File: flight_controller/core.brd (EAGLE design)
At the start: 94 x 90 mm, 102 parts, among them J1 M02, J13 MOLEX-3POS, J14 MOLEX-3POS, J15 MOLEX-4POS, J16 MOLEX-3POS, J17 M03, J18 M04, J19 MOLEX-3POS, J2 MOLEX-2POS, J20 MOLEX-4POS, J3 MOLEX-2POS, J4 MOLEX-2POS, J5 MOLEX-2POS, J6 MOLEX-2POS, J7 MOLEX-2POS, J8 MOLEX-2POS, J9 MOLEX-2POS, Q1 EM6K1, Q10 EM6K1, Q11 EM6K1, Q2 EM6K1, Q7 EM6K1, Q8 EM6K1, U1 MPU-6000QFN-24, U2 MEAS-MS5611, U3 USD-SOCKETNEW, U4 STM32F405, U5 MIC5219 3.3V, Y1 16MHz

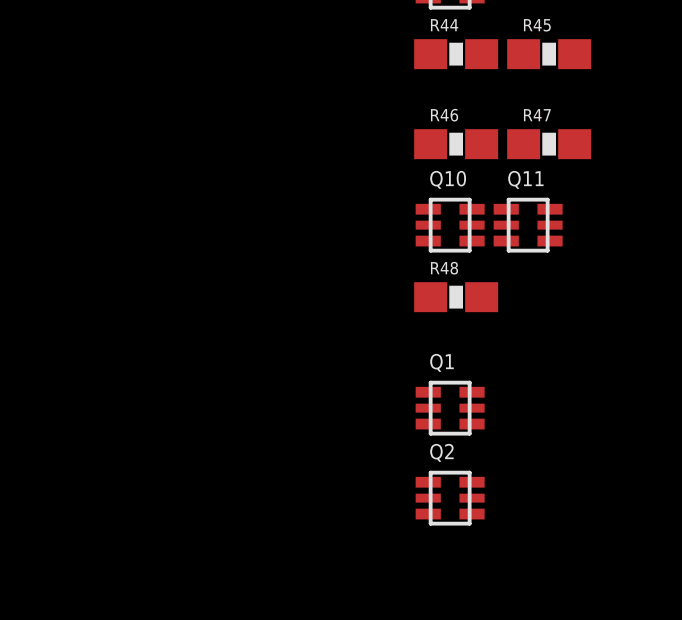
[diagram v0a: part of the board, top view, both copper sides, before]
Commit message: Remove 5V regulator todo and add reverse voltage protection.
Board will need 5V input from external regulator.
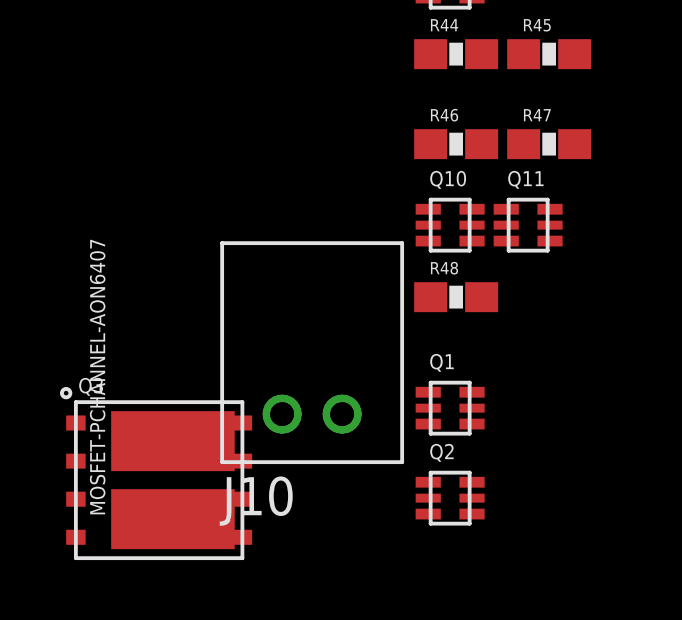
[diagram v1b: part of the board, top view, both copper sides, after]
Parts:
- added J10: MOLEX-2POS, aerial:MOLEX-2MM-MICROLATCH-2POS-RA
- added Q3: MOSFET-PCHANNEL-AON6407, OSURC_DiscreteSemi:DFN5X6
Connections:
- new net VIN: J10.1, Q3.5, Q3.6, Q3.7, Q3.8
- net 5V: now also Q3.1, Q3.2, Q3.3
- net GND: now also J10.2, Q3.4
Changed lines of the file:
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@@
 <attribute name="DIGIKEY_PN" value="EM6K1T2RCT-ND" x="-224" y="-588.9" size="1.778" layer="27" display="off"/>
+</element>
+<element name="J10" library="aerial" package="MOLEX-2MM-MICROLATCH-2POS-RA" value="MOLEX-2POS" x="-229.6" y="-586.1"/>
+<element name="Q3" library="OSURC_DiscreteSemi" package="DFN5X6" value="MOSFET-PCHANNEL-AON6407" x="-233.7" y="-588.3">
+<attribute name="DIGIKEY_PN" value="785-1421-1-ND" x="-233.7" y="-588.3" size="1.778" layer="27" display="off"/>
 </element>
 </elements>
@@
 <contactref element="Q1" pad="4"/>
 <contactref element="Q2" pad="1"/>
+<contactref element="J10" pad="2"/>
+<contactref element="Q3" pad="4"/>
 <wire x1="-127.4" y1="-372.6" x2="-136" y2="-372.6" width="0" layer="19" extent="1-1"/>
 <wire x1="-153.2" y1="-372.6" x2="-136" y2="-372.6" width="0" layer="19" extent="1-1"/>
@@
 <wire x1="-223.27" y1="-586.43" x2="-224.73" y2="-585.37" width="0" layer="19" extent="1-1"/>
 <wire x1="-224.73" y1="-588.37" x2="-223.27" y2="-586.43" width="0" layer="19" extent="1-1"/>
+<wire x1="-227.6" y1="-586.1" x2="-224.73" y2="-585.37" width="0" layer="19" extent="1-1"/>
+<wire x1="-236.475" y1="-590.205" x2="-227.6" y2="-586.1" width="0" layer="19" extent="1-1"/>
 <wire x1="-36.2" y1="-212.723" x2="-37.4" y2="-350.45" width="0" layer="19" extent="1-1"/>
 <wire x1="-33.3" y1="-209.623" x2="-36.2" y2="-212.723" width="0" layer="19" extent="1-1"/>
@@
 <contactref element="R33" pad="1"/>
 <contactref element="R34" pad="1"/>
+<contactref element="Q3" pad="1"/>
+<contactref element="Q3" pad="2"/>
+<contactref element="Q3" pad="3"/>
 <wire x1="-24.55" y1="-196.0001" x2="-30.65" y2="-222.5" width="0" layer="19" extent="1-1"/>
 <wire x1="-22.65" y1="-196.0001" x2="-24.55" y2="-196.0001" width="0" layer="19" extent="1-1"/>
@@
 <wire x1="-224.65" y1="-552.1" x2="-224.65" y2="-549.1" width="0" layer="19" extent="1-1"/>
 <wire x1="-224.65" y1="-555.1" x2="-224.65" y2="-552.1" width="0" layer="19" extent="1-1"/>
+<wire x1="-236.475" y1="-586.395" x2="-224.65" y2="-555.1" width="0" layer="19" extent="1-1"/>
+<wire x1="-236.475" y1="-587.665" x2="-236.475" y2="-586.395" width="0" layer="19" extent="1-1"/>
+<wire x1="-236.475" y1="-588.935" x2="-236.475" y2="-587.665" width="0" layer="19" extent="1-1"/>
 </signal>
 <signal name="ADC1-IN">
@@
 <contactref element="Q2" pad="2"/>
 </signal>
+<signal name="VIN">
+<contactref element="Q3" pad="5"/>
+<contactref element="Q3" pad="6"/>
+<contactref element="Q3" pad="7"/>
+<contactref element="Q3" pad="8"/>
+<contactref element="J10" pad="1"/>
+<wire x1="-230.925" y1="-588.935" x2="-230.925" y2="-590.205" width="0" layer="19" extent="1-1"/>
+<wire x1="-230.925" y1="-587.665" x2="-230.925" y2="-588.935" width="0" layer="19" extent="1-1"/>
+<wire x1="-230.925" y1="-586.395" x2="-230.925" y2="-587.665" width="0" layer="19" extent="1-1"/>
+<wire x1="-229.6" y1="-586.1" x2="-230.925" y2="-586.395" width="0" layer="19" extent="1-1"/>
+</signal>
 </signals>

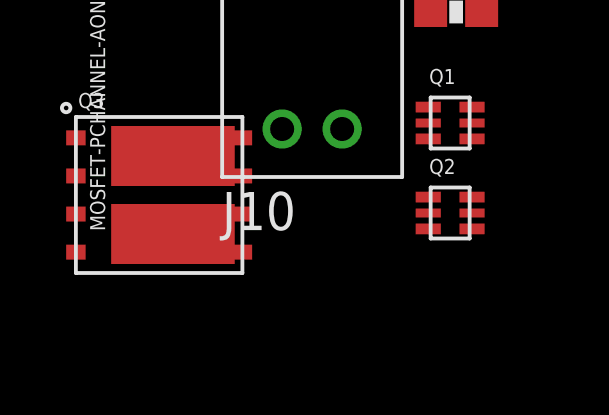
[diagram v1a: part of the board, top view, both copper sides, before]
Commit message: Add TVS/RVP circuit.
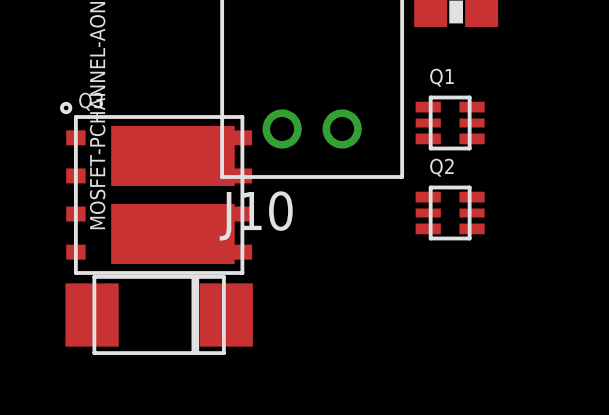
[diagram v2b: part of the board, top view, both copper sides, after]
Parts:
- added D1: DIODE-TVS-BIDIRECTIONAL-SMAJ12CA, OSURC_DiscreteSemi:SMAJ
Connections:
- net GND: now also D1.A
- net VIN: now also D1.C
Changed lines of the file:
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@@
 <attribute name="DIGIKEY_PN" value="785-1421-1-ND" x="-233.7" y="-588.3" size="1.778" layer="27" display="off"/>
+</element>
+<element name="D1" library="OSURC_DiscreteSemi" package="SMAJ" value="DIODE-TVS-BIDIRECTIONAL-SMAJ12CA" x="-233.7" y="-592.3">
+<attribute name="DIGIKEY_PN" value="SMAJ12CABCT-ND" x="-233.7" y="-592.3" size="1.778" layer="27" display="off"/>
 </element>
 </elements>
@@
 <contactref element="J10" pad="2"/>
 <contactref element="Q3" pad="4"/>
+<contactref element="D1" pad="A"/>
 <wire x1="-127.4" y1="-372.6" x2="-136" y2="-372.6" width="0" layer="19" extent="1-1"/>
 <wire x1="-153.2" y1="-372.6" x2="-136" y2="-372.6" width="0" layer="19" extent="1-1"/>
@@
 <wire x1="-227.6" y1="-586.1" x2="-224.73" y2="-585.37" width="0" layer="19" extent="1-1"/>
 <wire x1="-236.475" y1="-590.205" x2="-227.6" y2="-586.1" width="0" layer="19" extent="1-1"/>
+<wire x1="-235.9352" y1="-592.3" x2="-236.475" y2="-590.205" width="0" layer="19" extent="1-1"/>
 <wire x1="-36.2" y1="-212.723" x2="-37.4" y2="-350.45" width="0" layer="19" extent="1-1"/>
 <wire x1="-33.3" y1="-209.623" x2="-36.2" y2="-212.723" width="0" layer="19" extent="1-1"/>
@@
 </signal>
 <signal name="VIN">
+<contactref element="J10" pad="1"/>
 <contactref element="Q3" pad="5"/>
+<contactref element="Q3" pad="8"/>
+<contactref element="Q3" pad="7"/>
 <contactref element="Q3" pad="6"/>
-<contactref element="Q3" pad="7"/>
-<contactref element="Q3" pad="8"/>
-<contactref element="J10" pad="1"/>
+<contactref element="D1" pad="C"/>
+<wire x1="-230.925" y1="-590.205" x2="-231.4648" y2="-592.3" width="0" layer="19" extent="1-1"/>
 <wire x1="-230.925" y1="-588.935" x2="-230.925" y2="-590.205" width="0" layer="19" extent="1-1"/>
 <wire x1="-230.925" y1="-587.665" x2="-230.925" y2="-588.935" width="0" layer="19" extent="1-1"/>

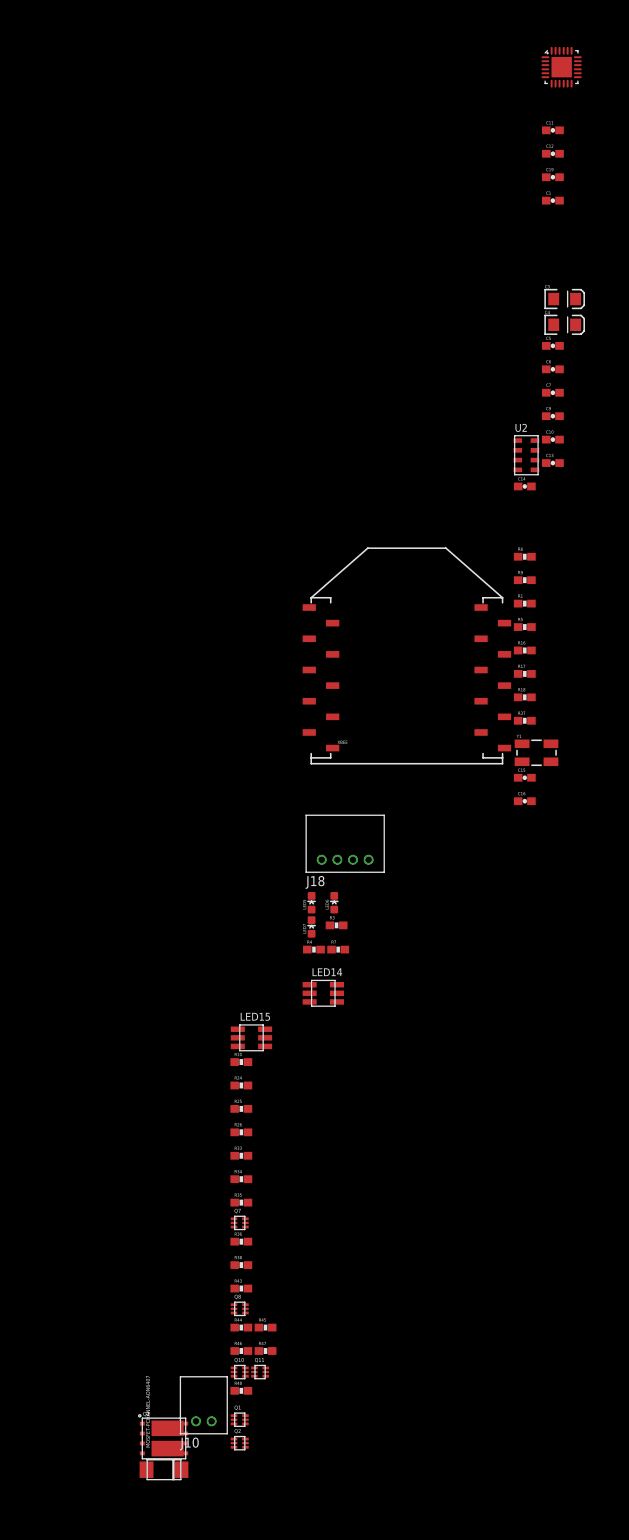
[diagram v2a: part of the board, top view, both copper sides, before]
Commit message: Implement MPU-9250.
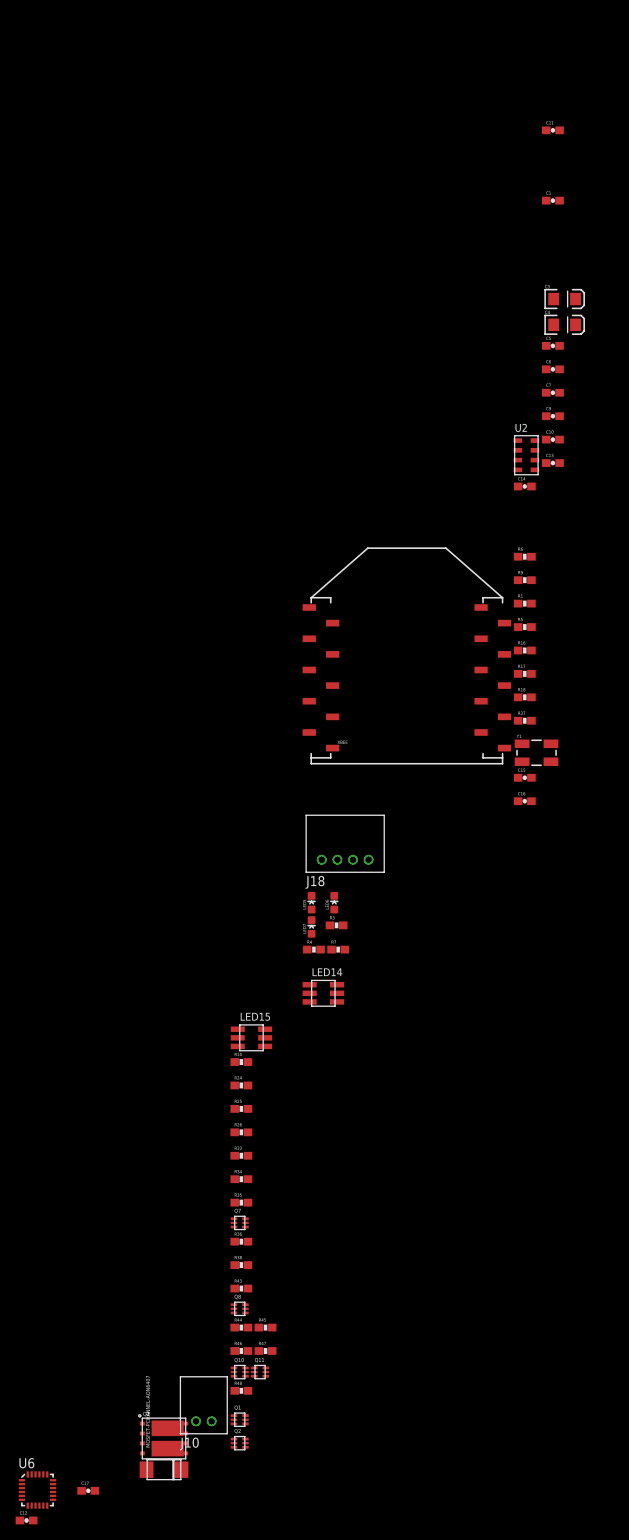
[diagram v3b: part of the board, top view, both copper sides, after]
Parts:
- removed C19: 2.2nF, SparkFun-Capacitors:0603-CAP
- removed U1: MPU-6000QFN-24, SparkFun-Sensors:QFN-24-TESTING
- added C17: 0.1uF, SparkFun-Capacitors:0603-CAP
- added U6: (no value), OSURC_Sensors:QFN-24-NP
- C12: value 0.1uF -> 10nF
- moved C12 187.5 mm to (-251.3, -598.8)
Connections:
- removed net MPU-CPOUT: C19.1, U1.20
- removed net MPU-REGOUT: C12.1, U1.10
- removed net SPISS-MPU6000: U1.8, U4.3
- new net MPU9250-REGOUT: C17.1, U6.10
- new net SPISS-MPU9250: U4.3, U6.22
- net 3.3V: now also C12.1, U6.1, U6.13, U6.8; no longer U1.13
- net GND: now also C17.2, U6.11, U6.18, U6.20; no longer C19.2, U1.18
- net SPI1-MISO: now also U6.9; no longer U1.9
- net SPI1-MOSI: now also U6.24; no longer U1.24
- net SPI1-SCK: now also U6.23; no longer U1.23

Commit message: Add digital I/O pins, remove some LEDs, rearrange stuff.
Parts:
- removed LED1, LED2, LED3, LED4: ORANGE, SparkFun-LED:LED-0603
- removed R14, R15, R21, R22: 680, SparkFun-Passives:0603-RES
- added J11, J12, J21, J22: MOLEX-2POS, aerial:MOLEX-2MM-MICROLATCH-2POS-RA
- moved XBEE 600.2 mm to (13.3, 58.2)
- moved U4 176.0 mm to (14.9, 11.7)
- moved U3 174.0 mm to (50.3, 20.8)
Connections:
- removed net N$27: LED2.A, R15.2
- removed net N$28: LED1.A, R14.2
- removed net N$29: LED3.A, R21.2
- removed net N$30: LED4.A, R22.2
- net GND: now also J11.2, J12.2, J21.2, J22.2; no longer LED1.C, LED2.C, LED3.C, LED4.C
- net PA4: now also J11.1; no longer R15.1
- net PA5: now also J12.1; no longer R14.1
- net PC4: now also J21.1; no longer R21.1
- net PC5: now also J22.1; no longer R22.1
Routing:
- net N$21: track 1.80 -> 0.00 mm
- net GND: track 0.10 -> 0.00 mm, vias 16 -> 0
- removed copper zone on layer 1, net GND
- removed copper zone on layer 16, net GND
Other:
- board outline removed
- board text removed: "5V GND NC"
- board text removed: "5V GND PA10"
- board text removed: "5V GND PA4"
- board text removed: "5V GND PA5"
- board text removed: "5V GND PC8"
- board text removed: "5V GND PC9"
- board text removed: "7V - 36V GND"
- board text removed: "DIN"
- board text removed: "DOUT"
- board text removed: "KILL"
- board text removed: "Oregon State University Autonomous Aerial Robotics Team 2014 Flight Control Board Rev 3"
- board text removed: "PA8 GND 5V"
- board text removed: "PB4"
- board text removed: "PB5"
- board text removed: "PC6 GND 5V"
- board text removed: "PC7 GND 5V"
- board text removed: "PWR"
- board text removed: "RSSI"
- board text removed: "RST"
- board text removed: "RST GND PA13 PA14"
- board text removed: "T G R"
- board text removed: "UART 1"
- board text removed: "UART 3"

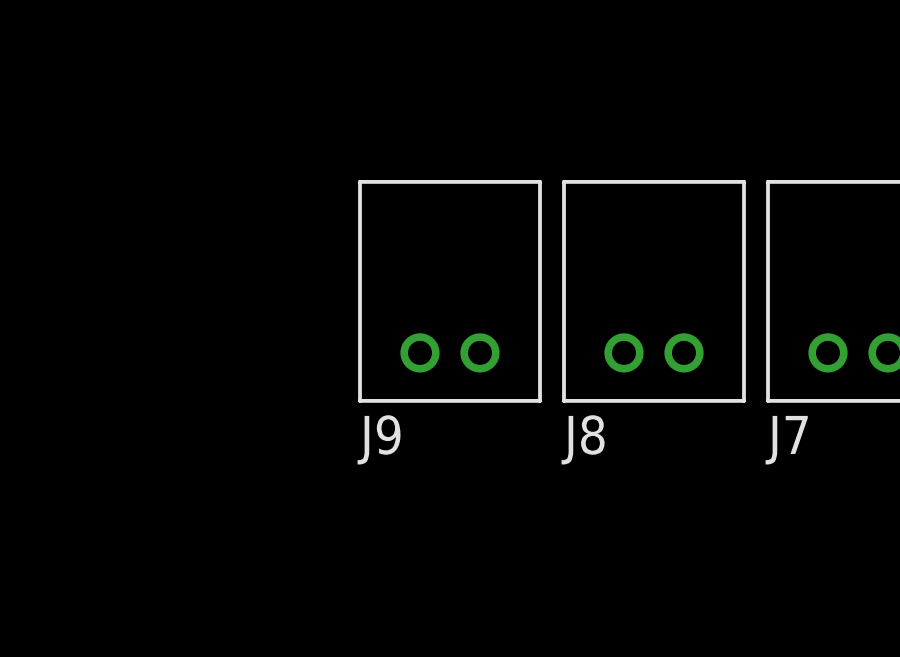
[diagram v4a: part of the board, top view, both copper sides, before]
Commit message: Resolve most ERC errors.
Two warnings for unused F4's B12 and C15.
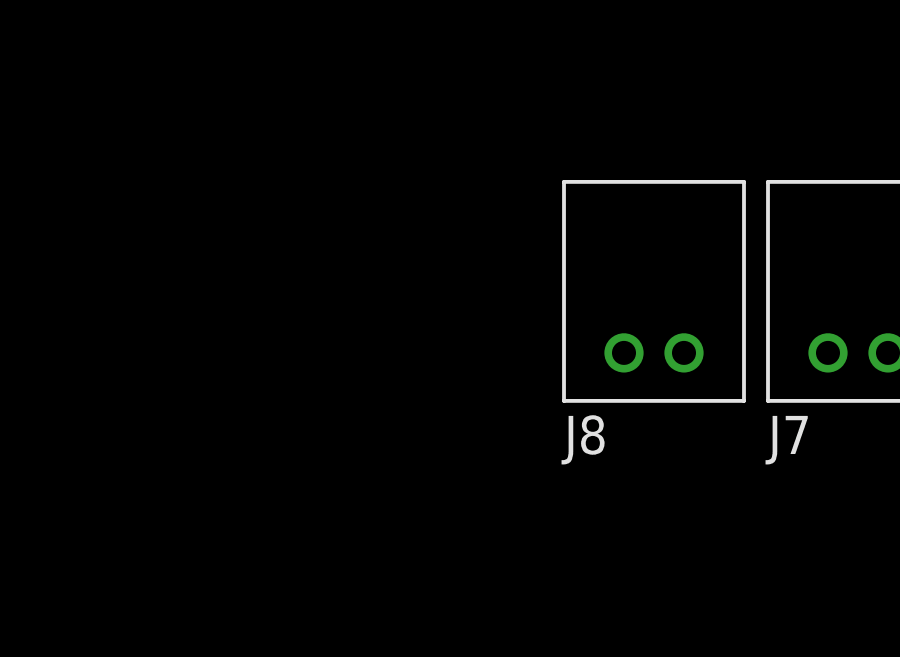
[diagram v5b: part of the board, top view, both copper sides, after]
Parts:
- removed J9: MOLEX-2POS, aerial:MOLEX-2MM-MICROLATCH-2POS-RA
- U6: value (none) -> MPU-9250-QFN-24-NP
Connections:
- removed net N$1: U3.4
- removed net TIM3-CH1: J9.1
- removed net TIM3-CH2-STSB: Q1.2
- removed net TIM3-CH4-STSR: Q2.2
- net 3.3V: now also U3.4; no longer J13.2, J14.2
- net 5V: now also J13.2, J14.2
- net GND: no longer J9.2
- net TIM3-CH2-STSR: now also Q2.2
- net TIM3-CH4-STSB: now also Q1.2
